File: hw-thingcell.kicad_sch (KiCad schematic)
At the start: 39 parts, among them J1 Conn_01x02_Pin, J2 Conn_Coaxial, J3 SIM_Card, K1 JRC-21F(4100), Q1 PMBT3904235, Q2 PMBT3904235, U1 ESP32-WROOM-32, U2 SIM800C, U3 NCP1117-3.3_SOT223

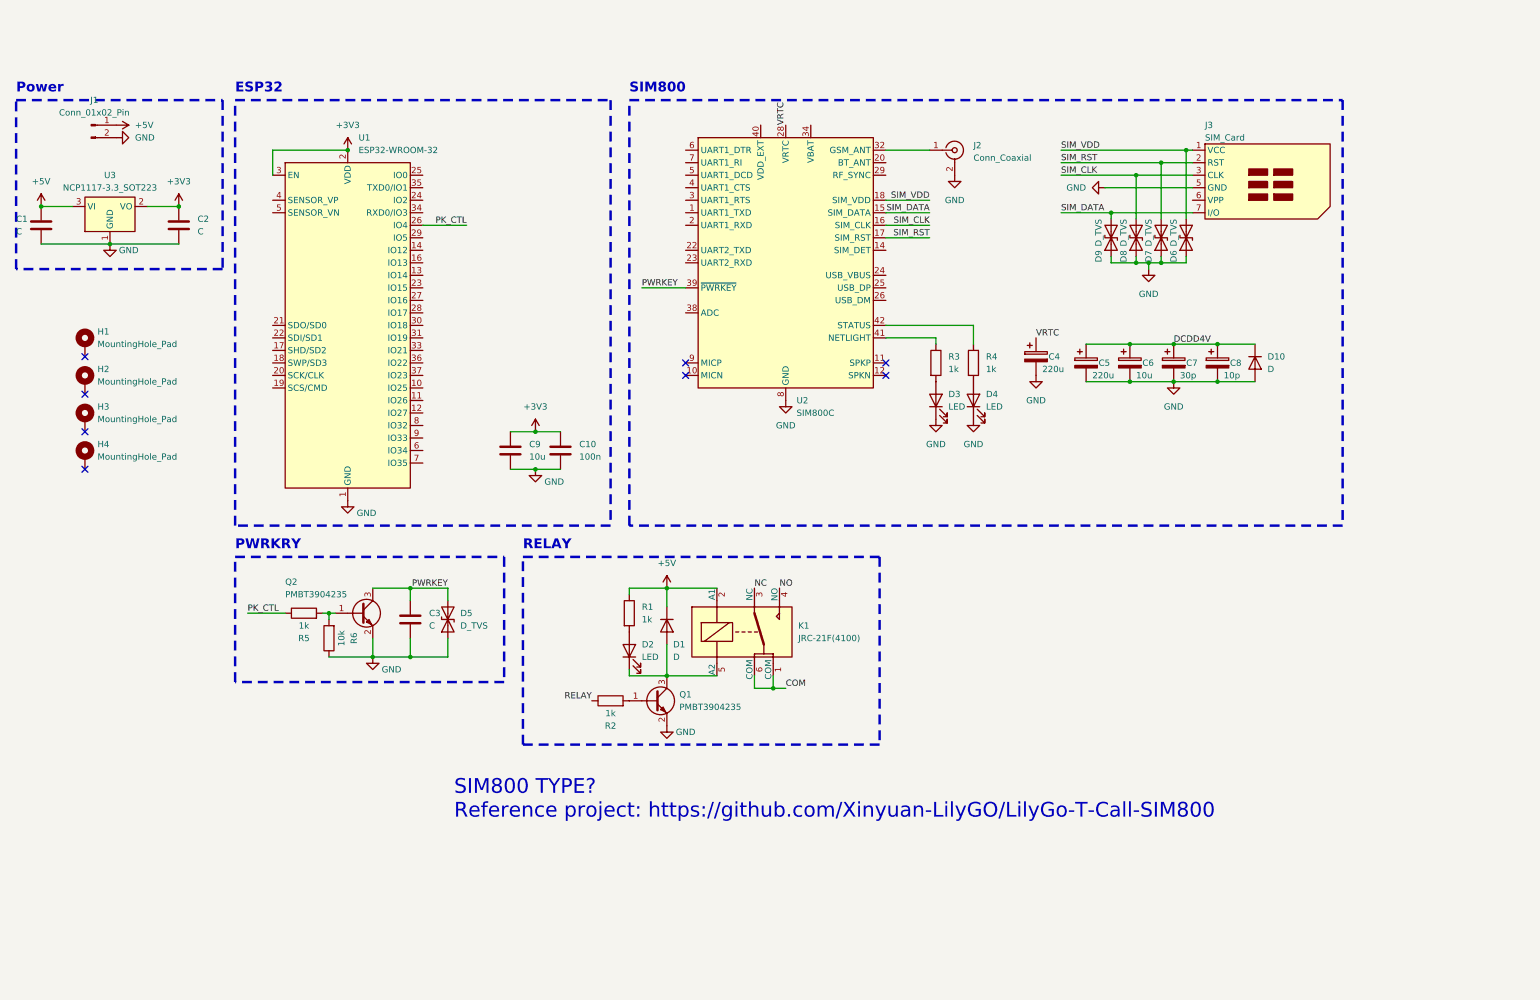
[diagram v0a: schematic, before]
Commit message: Continue with schematic adding ESP and SIM components
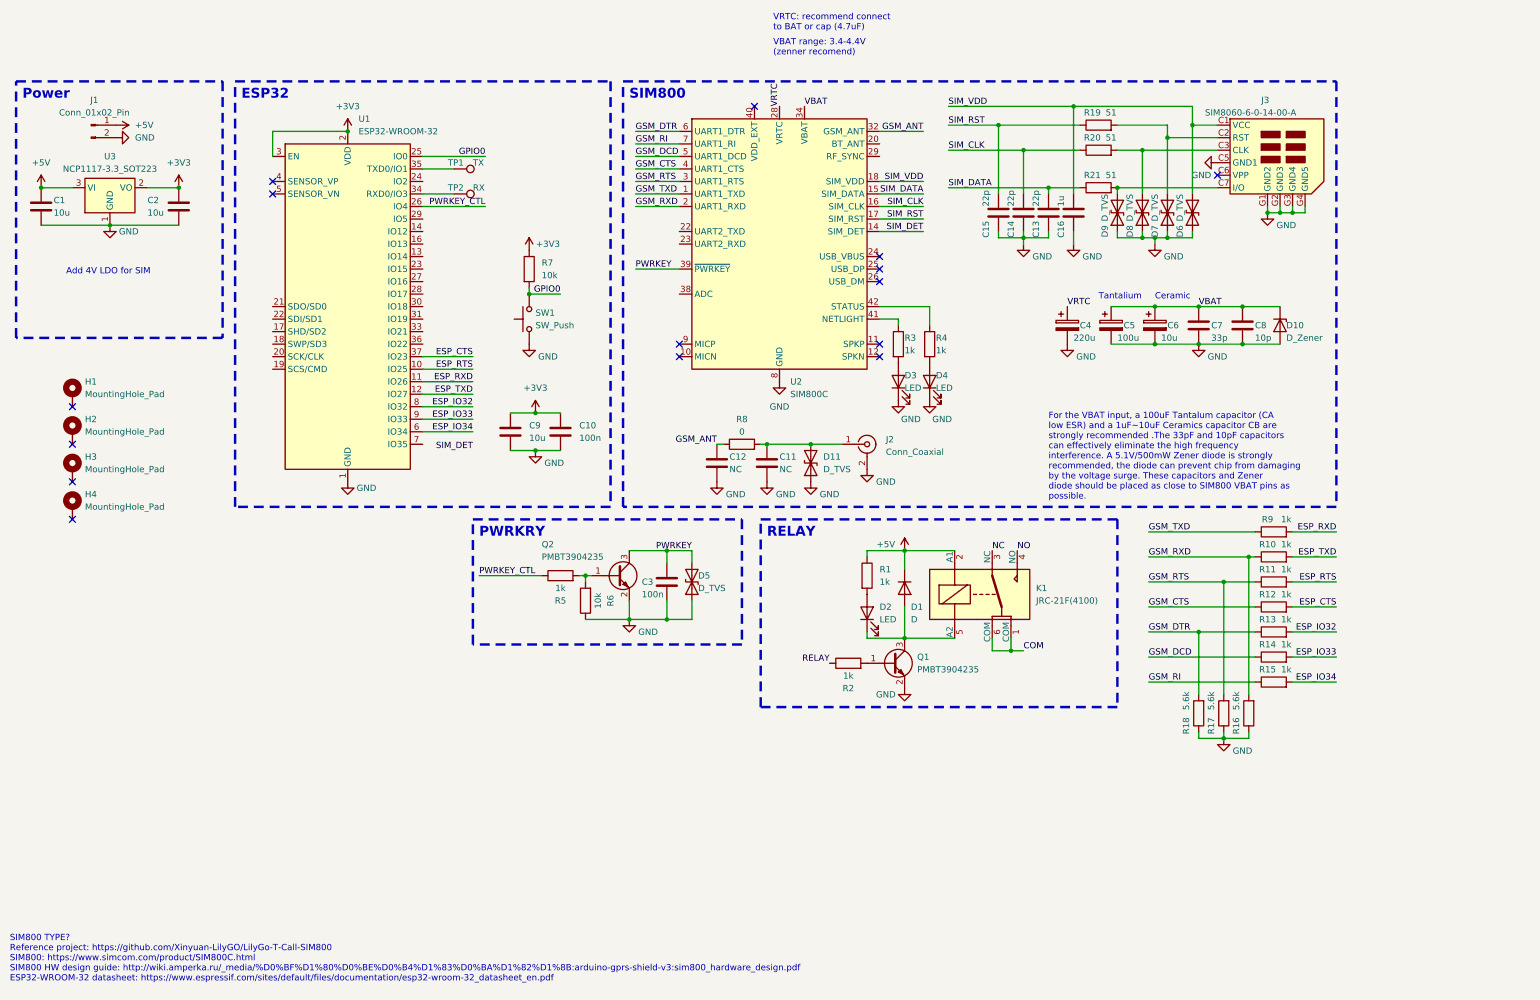
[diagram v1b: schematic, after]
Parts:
- removed C7: 30p, symbol Device:C_Polarized
- removed C8: 10p, symbol Device:C_Polarized
- removed D10: D, symbol Device:D
- removed J3: SIM_Card, symbol Connector:SIM_Card
- added C11, C12: NC, Capacitor_SMD:C_0402_1005Metric, symbol Device:C
- added C13, C14, C15: 22p, Capacitor_SMD:C_0402_1005Metric, symbol Device:C
- added C16: 1u, symbol Device:C
- added C7: 33p, Capacitor_SMD:C_0402_1005Metric, symbol Device:C
- added C8: 10p, Capacitor_SMD:C_0402_1005Metric, symbol Device:C
- added D10: D_Zener, symbol Device:D_Zener
- added D11: D_TVS, Diode_SMD:D_0402_1005Metric, symbol Device:D_TVS
- added J3: SIM8060-6-0-14-00-A, guille-lib:SIM8060601400A, symbol guille-lib:SIM8060-6-0-14-00-A
- added R10, R11, R12, R13, R14, R15, R9: 1k, Resistor_SMD:R_0402_1005Metric, symbol Device:R
- added R16, R17, R18: 5.6k, Resistor_SMD:R_0402_1005Metric, symbol Device:R
- added R19, R20, R21: 51, Resistor_SMD:R_0402_1005Metric, symbol Device:R
- added R7: 10k, Resistor_SMD:R_0402_1005Metric, symbol Device:R
- added R8: 0, Resistor_SMD:R_0402_1005Metric, symbol Device:R
- added SW1: SW_Push, symbol Switch:SW_Push
- added TP1: TX, TestPoint:TestPoint_Pad_D1.0mm, symbol Connector:TestPoint
- added TP2: RX, TestPoint:TestPoint_Pad_D1.0mm, symbol Connector:TestPoint
- C1, C2: value C -> 10u
- C10: footprint (none) -> Capacitor_SMD:C_0402_1005Metric
- C3: value C -> 100n; footprint (none) -> Capacitor_SMD:C_0402_1005Metric
- C5: value 220u -> 100u
- D2, D3, D4: footprint (none) -> LED_SMD:LED_0402_1005Metric
- D5, D6, D7, D8, D9: footprint (none) -> Diode_SMD:D_0402_1005Metric
- H1, H2, H3, H4: footprint (none) -> MountingHole:MountingHole_2.2mm_M2_Pad
- J1: footprint (none) -> Connector_PinHeader_2.54mm:PinHeader_1x02_P2.54mm_Vertical
- R1, R2, R3, R4, R5, R6: footprint (none) -> Resistor_SMD:R_0402_1005Metric
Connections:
- net DCDD4V is gone; now on net VBAT: C5.1, C6.1
- net +3V3: now also R7.1
- net GND: now also C11.2, C12.2, C13.2, C14.2, C15.2, C16.2, C7.2, C8.2, D10.2 (A), D11.1 (A1), J3.C5 (GND1), J3.G1 (GND2), J3.G2 (GND3), J3.G3 (GND4), J3.G4 (GND5), R16.1, R17.1, R18.1, SW1.1
- net SIM_CLK: now also C14.1, R20.1; no longer D8.2 (A2)
- net SIM_DATA: now also C13.1, R21.1; no longer D9.2 (A2)
- net SIM_RST: now also C15.1, R19.1; no longer D7.2 (A2)
- net SIM_VDD: now also C16.1, J3.C1 (VCC)
- net GSM_TXD: now reaches U2.1 (UART1_TXD)
- net GSM_TXD: now also R9.1
- net SIM_DET: now reaches U2.14 (SIM_DET)
- net GSM_RXD: now reaches U2.2 (UART1_RXD)
- net GSM_RXD: now also R10.1, R16.2
- net GSM_RTS: now reaches U2.3 (UART1_RTS)
- net GSM_RTS: now also R11.1, R17.2
- net at J2.1 (In): now also C11.1, D11.2 (A2), R8.2; no longer U2.32 (GSM_ANT)
- net VBAT: now reaches U2.34 (VBAT), U2.35 (VBAT)
- net VBAT: now also C7.1, C8.1, D10.1 (K)
- net GSM_CTS: now reaches U2.4 (UART1_CTS)
- net GSM_CTS: now also R12.1
- net GSM_DCD: now reaches U2.5 (UART1_DCD)
- net GSM_DCD: now also R14.1
- net GSM_DTR: now reaches U2.6 (UART1_DTR)
- net GSM_DTR: now also R13.1, R18.2
- net GSM_RI: now reaches U2.7 (UART1_RI)
- net GSM_RI: now also R15.1
- net ESP_RTS: now reaches U1.10 (IO25)
- net ESP_RTS: now also R11.2
- net ESP_RXD: now reaches U1.11 (IO26)
- net ESP_RXD: now also R9.2
- net ESP_TXD: now reaches U1.12 (IO27)
- net ESP_TXD: now also R10.2
- net GPIO0: now reaches U1.25 (IO0)
- net GPIO0: now also R7.2, SW1.2
- net at U1.34 (RXD0/IO3): now also TP2.1
- net at U1.35 (TXD0/IO1): now also TP1.1
- net ESP_CTS: now reaches U1.37 (IO23)
- net ESP_CTS: now also R12.2
- net ESP_IO34: now reaches U1.6 (IO34)
- net ESP_IO34: now also R15.2
- net ESP_IO32: now reaches U1.8 (IO32)
- net ESP_IO32: now also R13.2
- net ESP_IO33: now reaches U1.9 (IO33)
- net ESP_IO33: now also R14.2
- net PK_CTL renamed PWRKEY_CTL
- new net: D7.2 (A2), J3.C2 (RST), R19.2
- new net: D8.2 (A2), J3.C3 (CLK), R20.2
- new net: D9.2 (A2), J3.C7 (I/O), R21.2
- new net GSM_ANT: C12.1, R8.1, U2.32 (GSM_ANT)
- no-connect marks 8 -> 15
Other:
- note added: "Add 4V LDO for SIM"
- note added: "Ceramic"
- note added: "For the VBAT input, a 100uF Tantalum capacitor (CA low ESR) and a 1uF~10uF Ceramics capacitor CB are strongly recommended .The 33pF and 10pF capacitors can effectively eliminate the high frequency interference. A 5.1V/500mW Zener diode is strongly recommended, the diode can prevent chip from damaging by the voltage surge. These capacitors and Zener diode should be placed as close to SIM800 VBAT p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"
- note added: "SIM800 TYPE? Reference project: https://github.com/Xinyuan-LilyGO/LilyGo-T-Call-SIM800 SIM800: https://www.simcom.com/product/SIM800C.html SIM800 HW design guide: http://wiki.amperka.ru/_media/%D0%BF%D1%80%D0%BE%D0%B4%D1%83%D0%BA%D1%82%D1%8B:arduino-gprs-shield-v3:sim800_hardware_design.pdf ESP32-WROOM-32 datasheet: https://www.espressif.com/sites/default/files/documentation/esp32-wroom-32_datash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"
- note added: "Tantalium"
- note added: "VBAT range: 3.4-4.4V (zenner recomend)"
- note added: "VRTC: recommend connect to BAT or cap (4.7uF)"
- note removed: "SIM800 TYPE? Reference project: https://github.com/Xinyuan-LilyGO/LilyGo-T-Call-SIM800"
- moved on the sheet: C1, C10, C2, C3, C4, C5, C6, C9, D1, D2, D3, D4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

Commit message: Work on schematic
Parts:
- added J4: Conn_01x08_Pin, symbol Connector:Conn_01x08_Pin
- added TP3: GND, TestPoint:TestPoint_Pad_D1.0mm, symbol Connector:TestPoint
- added TP4: 3V3, TestPoint:TestPoint_Pad_D1.0mm, symbol Connector:TestPoint
- U2: footprint RF_GSM:SIMCom_SIM800C -> guille-lib:SIM800C; symbol RF_GSM:SIM800C -> guille-lib:SIM800C
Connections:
- net +3V3: now also J4.2 (Pin_2), TP4.1
- net +5V: now also J4.1 (Pin_1)
- net GND: now also J4.8 (Pin_8), TP3.1
- net RX: now reaches TP2.1, U1.34 (RXD0/IO3)
- net TX: now reaches TP1.1, U1.35 (TXD0/IO1)
- net PWRKEY_CTL renamed PK_CTL
- new net GPIO1: J4.5 (Pin_5)
- new net GPIO2: J4.6 (Pin_6)
- new net GPIO3: J4.7 (Pin_7)
- new net I2C_SCL: J4.4 (Pin_4)
- new net I2C_SDA: J4.3 (Pin_3)
- no-connect marks 15 -> 17
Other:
- note added: "Boton, XTOR, RELE, DIODOS: comprobar en la oficina TENEMOS TVS ENCAPSULADOS EN LA OFICINA? Quito el filtro de la antena (datasheet dice que la mayoria de las veces es C:NC,R:0) ADC SIM bateria??"
- note added: "Expansion port"
- moved on the sheet: C11, C12, C3, D1, D11, D2, D5, J2, K1, Q1, Q2, R1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
